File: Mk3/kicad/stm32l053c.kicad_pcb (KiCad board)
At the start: 2 copper layers, 26.7 x 43.2 mm, 44 parts, among them J1 GND, J2 GND, J3 TX, J4 GND, J5 TEST_1P, J6 TEST_1P, J7 TEST_1P, J8 RX, P1 SWD, U1 AP2112, U2 STM32L053C8_LQFP48, U3 ADS1015, U4 UFL_SMA, U5 RFM92/95

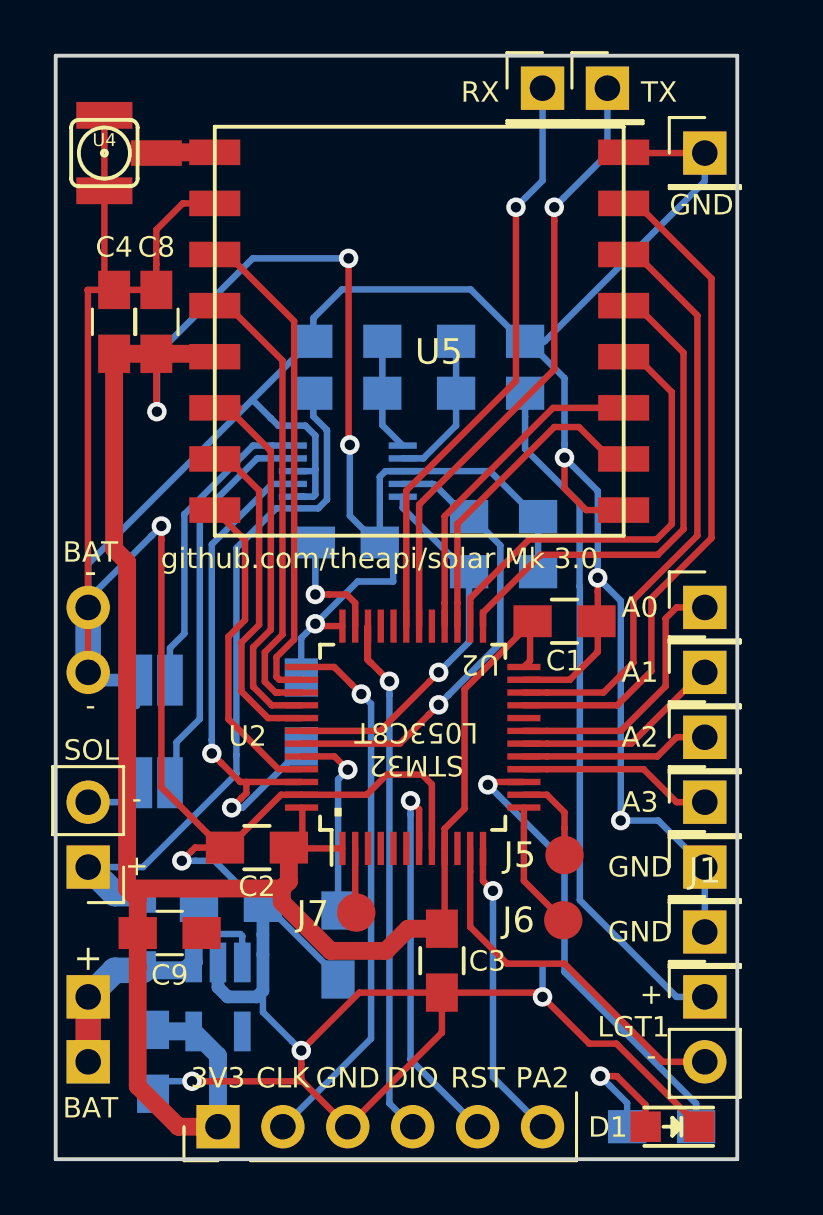
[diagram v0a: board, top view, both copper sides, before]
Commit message: Moved a couple of resistors
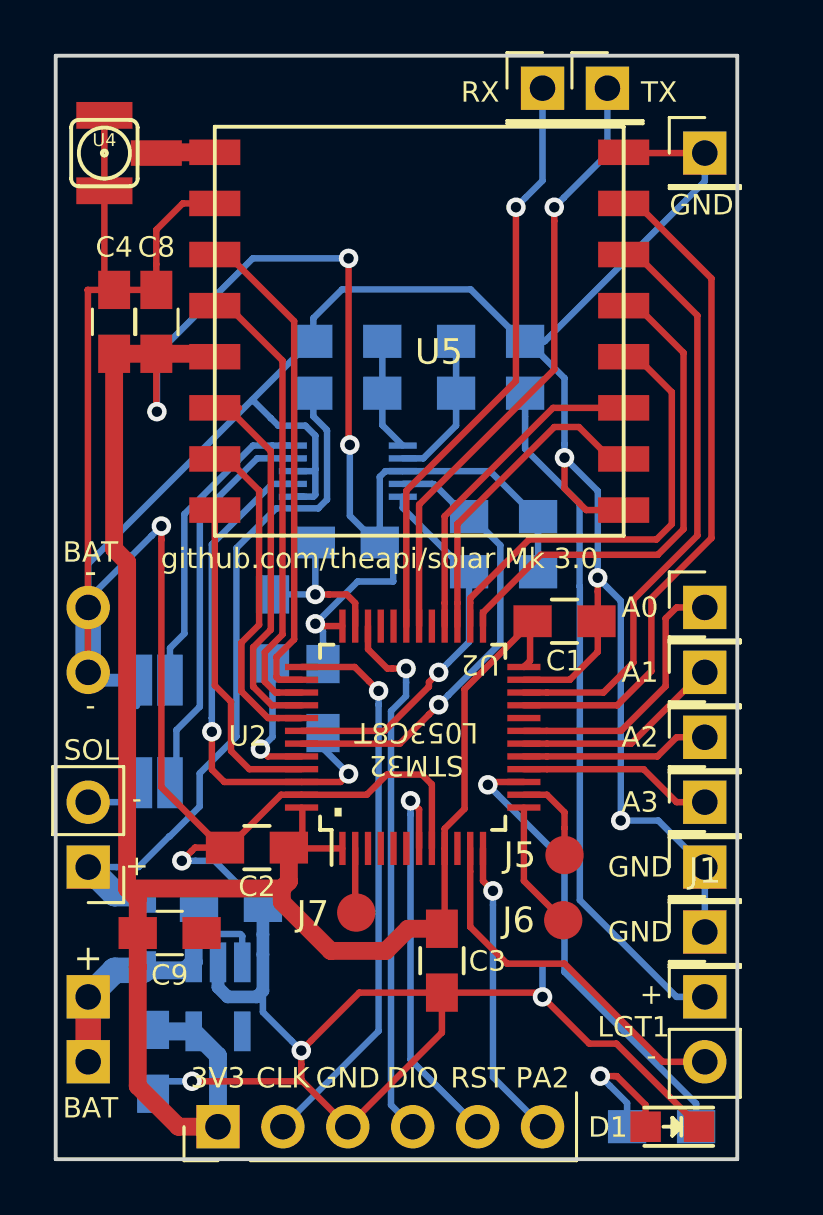
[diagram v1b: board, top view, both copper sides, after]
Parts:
- moved R4 12.6 mm to (144.4, 74.5), turned to 90 degrees
- moved R10 1.00 mm to (146.3, 77.2)
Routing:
- net /BOOT0: track 7.69 -> 5.28 mm
- net Earth: track 215.9 -> 213.5 mm
- net SWCLK: track 21.3 -> 22.0 mm
- net ADC_RDY: track 21.3 -> 20.7 mm
- net +3V3: track 127.5 -> 126.9 mm
- net SWDIO: track 21.8 -> 21.2 mm

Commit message: Pull up resistor for the DS18B20 one wire temperature sensor
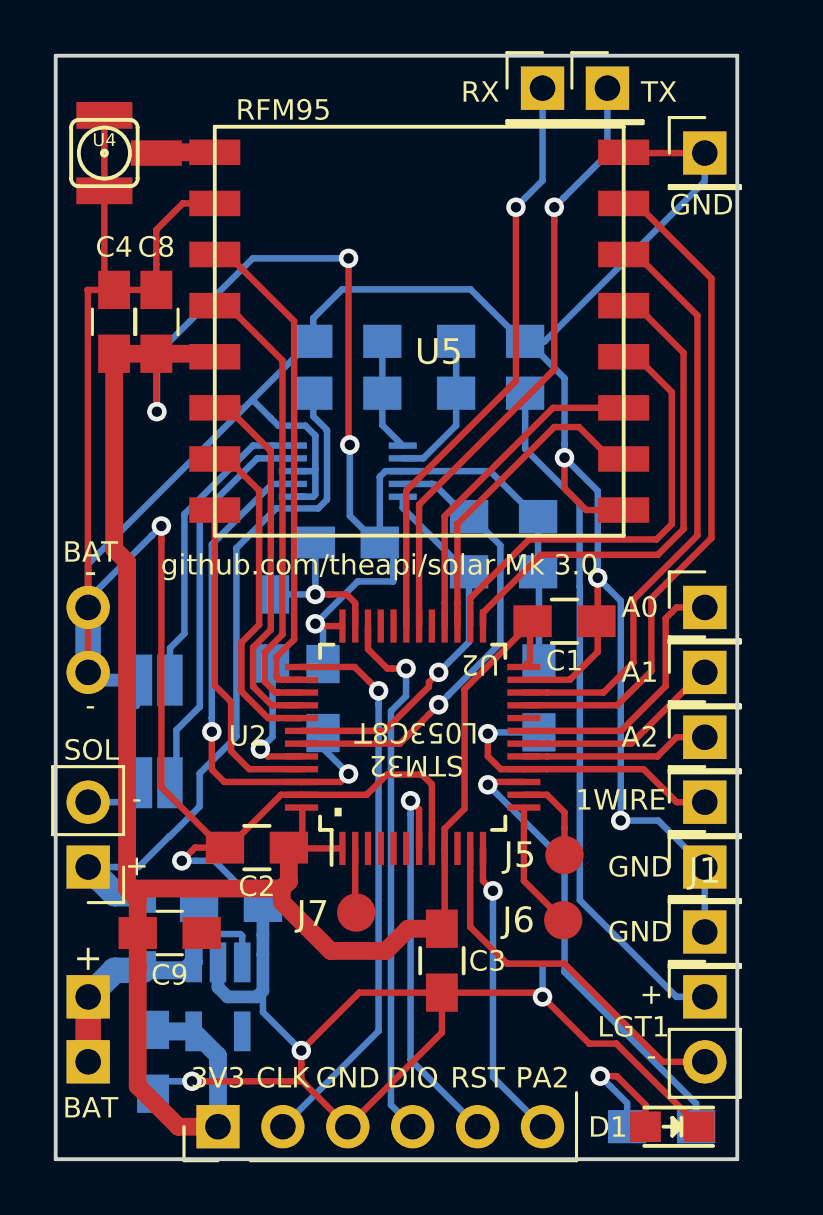
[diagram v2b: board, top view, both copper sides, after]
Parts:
- removed A3: A3, Pin_Headers:Pin_Header_Straight_1x01_Pitch2.54mm
- added PA6: A3, Pin_Headers:Pin_Header_Straight_1x01_Pitch2.54mm, F.Cu at (161.3, 81.3)
- added R11: 4K7, Resistors_SMD:R_0805_HandSoldering, B.Cu at (154.8, 77.2)
- moved REF** 1.20 mm to (142.6, 53.6)
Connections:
- U2 pad 16: Net-(A3-Pad1) -> /1_WIRE
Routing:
- net /1_WIRE: track 0.00 -> 12.1 mm, vias 0 -> 1
- net Net-(A3-Pad1): track 7.61 -> 0.00 mm
- net +3V3: track 126.9 -> 130.5 mm
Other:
- board text added: "1WIRE"
- board text added: "ADS1015"
- board text added: "RFM95"
- board text removed: "A3"

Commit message: Extra 3v3 pins
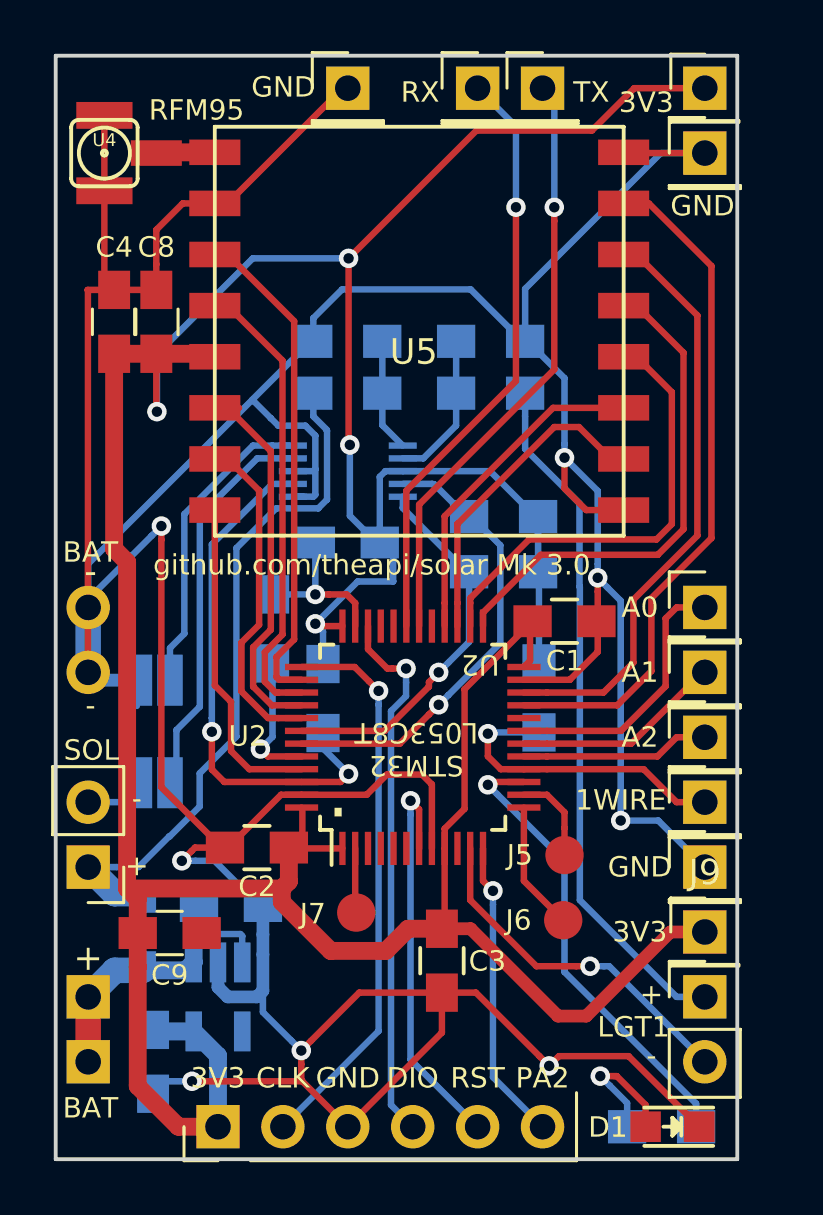
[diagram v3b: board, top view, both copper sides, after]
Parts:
- added J10: 3V3, Pin_Headers:Pin_Header_Straight_1x01_Pitch2.54mm, F.Cu at (161.3, 53.3)
- added J9: 3V3, Pin_Headers:Pin_Header_Straight_1x01_Pitch2.54mm, F.Cu at (161.3, 86.4)
- moved J1 35.9 mm to (147.3, 53.3)
- moved J3 2.54 mm to (154.9, 53.3)
- moved J8 2.54 mm to (152.4, 53.3)
- moved REF** 1.77 mm to (141.3, 54.8)
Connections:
- U1 pad 4: Net-(U1-Pad4) -> (no net)
- U2 pad 10: Net-(U2-Pad10) -> (no net)
- U2 pad 20: Net-(U2-Pad20) -> (no net)
- U2 pad 29: Net-(U2-Pad29) -> (no net)
- U2 pad 3: Net-(U2-Pad3) -> (no net)
- U2 pad 32: Net-(U2-Pad32) -> (no net)
- U2 pad 33: Net-(U2-Pad33) -> (no net)
- U2 pad 4: Net-(U2-Pad4) -> (no net)
- U2 pad 5: Net-(U2-Pad5) -> (no net)
- U2 pad 6: Net-(U2-Pad6) -> (no net)
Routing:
- net +3V3: track 130.5 -> 160.2 mm
- net Earth: track 213.5 -> 217.5 mm
- net USART1_TX: track 24.1 -> 23.4 mm
- net LGT_GND: track 14.4 -> 13.9 mm, vias 0 -> 1

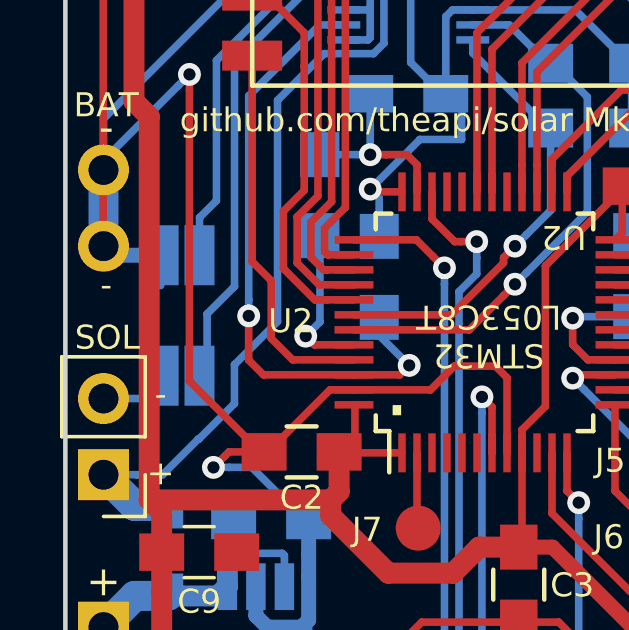
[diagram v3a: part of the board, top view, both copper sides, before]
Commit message: Shunt footprint change
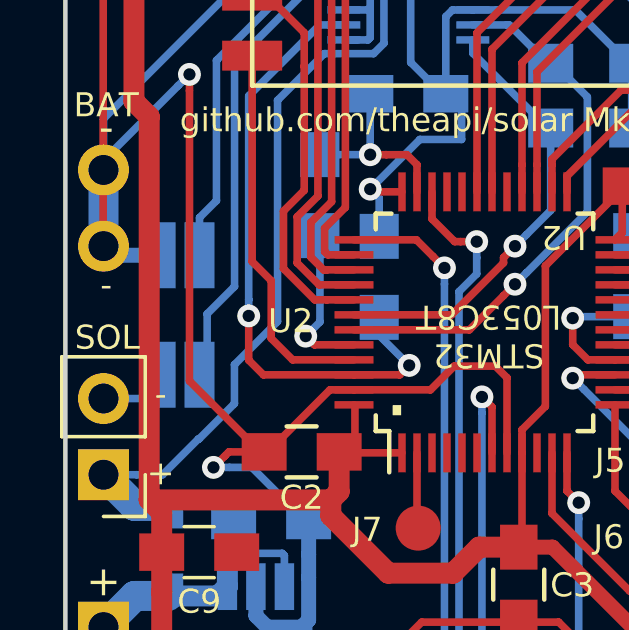
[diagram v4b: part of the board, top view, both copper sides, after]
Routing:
- net Earth: track 217.5 -> 216.5 mm
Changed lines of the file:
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@@
-(kicad_pcb (version 4) (host pcbnew 4.0.6-e0-6349~53~ubuntu16.04.1)
+(kicad_pcb (version 4) (host pcbnew 4.0.6)
   (general
     (links 104)
     (no_connects 0)
-    (area 135.814999 51.994999 162.635001 95.325001)
+    (area 112.673333 49.811 163.369001 97.209)
     (thickness 1.6)
     (drawings 61)
-    (tracks 512)
+    (tracks 511)
     (zones 0)
     (modules 47)
@@
       (scale (xyz 1 1 1))
       (rotate (xyz 0 0 90))
-    )
-  )
-  (module theapi:SHUNT_1210_HandSoldering (layer B.Cu)
-    (at 139.7 78.486 90)
-    (descr "Resistor SMD 1210, hand soldering")
-    (tags "resistor 1210")
-    (clearance 0.05)
-    (attr smd)
-    (fp_text reference R5 (at -0.014 2.3 180) (layer B.SilkS)
-      (effects (font (size 0.8 0.8) (thickness 0.15)) (justify mirror))
-    )
-    (fp_text value R_Shunt (at 0 -2.4 90) (layer B.Fab)
-      (effects (font (size 1 1) (thickness 0.15)) (justify mirror))
-    )
-    (fp_text user %R (at 0 2.3 90) (layer B.Fab)
-      (effects (font (size 1 1) (thickness 0.15)) (justify mirror))
-    )
-    (fp_line (start -1.6 -1.25) (end -1.6 1.25) (layer B.Fab) (width 0.1))
-    (fp_line (start 1.6 -1.25) (end -1.6 -1.25) (layer B.Fab) (width 0.1))
-    (fp_line (start 1.6 1.25) (end 1.6 -1.25) (layer B.Fab) (width 0.1))
-    (fp_line (start -1.6 1.25) (end 1.6 1.25) (layer B.Fab) (width 0.1))
-    (fp_line (start 1 -1.48) (end -1 -1.48) (layer B.SilkS) (width 0.12))
-    (fp_line (start -1 1.48) (end 1 1.48) (layer B.SilkS) (width 0.12))
-    (fp_line (start -3.25 1.5) (end 3.25 1.5) (layer B.CrtYd) (width 0.05))
-    (fp_line (start -3.25 1.5) (end -3.25 -1.5) (layer B.CrtYd) (width 0.05))
-    (fp_line (start 3.25 -1.5) (end 3.25 1.5) (layer B.CrtYd) (width 0.05))
-    (fp_line (start 3.25 -1.5) (end -3.25 -1.5) (layer B.CrtYd) (width 0.05))
-    (pad 4 smd rect (at 1.9812 -0.635 90) (size 2 1.2) (layers B.Cu B.Paste B.Mask)
-      (net 1 Earth))
-    (pad 1 smd rect (at -2.032 -0.635 90) (size 2 1.2) (layers B.Cu B.Paste B.Mask)
-      (net 25 SOL_GND))
-    (pad 2 smd rect (at -2.032 0.6604 90) (size 2 1) (layers B.Cu B.Paste B.Mask)
-      (net 23 /AIN0))
-    (pad 3 smd rect (at 1.9812 0.6604 90) (size 2 1) (layers B.Cu B.Paste B.Mask)
-      (net 26 /AIN1))
-    (model Resistors_SMD.3dshapes/R_1210.wrl
-      (at (xyz 0 0 0))
-      (scale (xyz 1 1 1))
-      (rotate (xyz 0 0 0))
     )
   )
@@
     )
   )
+  (module theapi:SHUNT_1210_HandSoldering (layer B.Cu)
+    (at 139.7 78.486 90)
+    (descr "Resistor SMD 1210, hand soldering")
+    (tags "resistor 1210")
+    (clearance 0.05)
+    (attr smd)
+    (fp_text reference R5 (at -0.014 2.3 180) (layer B.SilkS)
+      (effects (font (size 0.8 0.8) (thickness 0.15)) (justify mirror))
+    )
+    (fp_text value R_Shunt (at 0 -2.4 90) (layer B.Fab)
+      (effects (font (size 1 1) (thickness 0.15)) (justify mirror))
+    )
+    (fp_text user %R (at 0 2.3 90) (layer B.Fab)
+      (effects (font (size 1 1) (thickness 0.15)) (justify mirror))
+    )
+    (fp_line (start -3.25 1.25) (end 3.25 1.25) (layer B.CrtYd) (width 0.05))
+    (fp_line (start -3.25 1.25) (end -3.25 -1.25) (layer B.CrtYd) (width 0.05))
+    (fp_line (start 3.25 -1.25) (end 3.25 1.25) (layer B.CrtYd) (width 0.05))
+    (fp_line (start 3.25 -1.25) (end -3.25 -1.25) (layer B.CrtYd) (width 0.05))
+    (pad 4 smd rect (at 1.9812 -0.635 90) (size 2.2 1) (layers B.Cu B.Paste B.Mask)
+      (net 1 Earth))
+    (pad 1 smd rect (at -2 -0.635 90) (size 2.2 1) (layers B.Cu B.Paste B.Mask)
+      (net 25 SOL_GND))
+    (pad 2 smd rect (at -2 0.6604 90) (size 2.2 1) (layers B.Cu B.Paste B.Mask)
+      (net 23 /AIN0))
+    (pad 3 smd rect (at 1.9812 0.6604 90) (size 2.2 1) (layers B.Cu B.Paste B.Mask)
+      (net 26 /AIN1))
+    (model Resistors_SMD.3dshapes/R_1210.wrl
+      (at (xyz 0 0 0))
+      (scale (xyz 1 1 1))
+      (rotate (xyz 0 0 0))
+    )
+  )
   (gr_text 3V3 (at 159 53.9) (layer B.SilkS)
     (effects (font (size 0.8 0.8) (thickness 0.15)) (justify mirror))
@@
   (segment (start 139.065 76.5048) (end 137.4648 76.5048) (width 0.5) (layer B.Cu) (net 1))
   (segment (start 137.4648 76.5048) (end 137.16 76.2) (width 0.5) (layer B.Cu) (net 1))
-  (segment (start 139.065 76.5048) (end 139.065 77.515001) (width 0.254) (layer B.Cu) (net 1))
   (segment (start 148.85 80.2) (end 148.06 80.99) (width 0.254) (layer F.Cu) (net 1))
   (segment (start 148.06 80.99) (end 145.51 80.99) (width 0.254) (layer F.Cu) (net 1))
